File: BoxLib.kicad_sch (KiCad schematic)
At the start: 18 parts, among them J1 Generic_2Pos_terminal_block, J10 Molex_2Pos_terminal_block_1.2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, J11 Generic_2Pos_terminal_block, J2 Solder-Jumper-NO, J3 Solder-Jumper-NO, J4 Solder-Jumper-NO, J5 Solder-Jumper-NC, J6 Solder-Jumper-NC, J7 Solder-Jumper-NC, J8 Solder-Jumper-NO, J9 Solder-Jumper-NC, U1 QT_Py_RP2040, U2 QT_Py

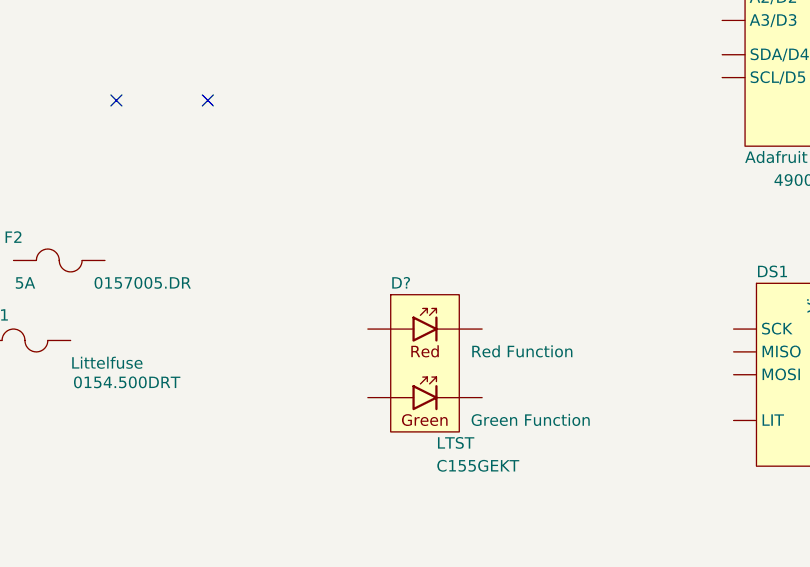
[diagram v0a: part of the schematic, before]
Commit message: Added PTH varients of devices
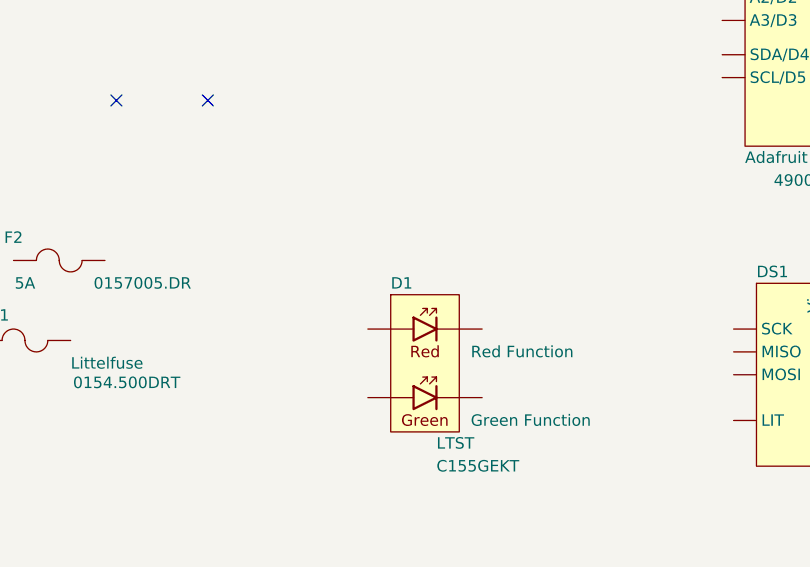
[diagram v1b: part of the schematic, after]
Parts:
- gave numbers to parts that had none: 1
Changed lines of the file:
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@@
   (symbol (lib_id "BoxLib-LEDs:LED-LTST-C155GEKT") (at 154.94 105.41 0) (unit 1)
     (in_bom yes) (on_board yes)
-    (property "Reference" "D?" (id 0) (at 151.13 96.52 0)
+    (property "Reference" "D1" (id 0) (at 151.13 96.52 0)
       (effects (font (size 1.27 1.27)) (justify left))
     )
@@
   (symbol_instances
     (path "/cfdfa8c8-35d8-45dc-a3f3-e836c8fa5543"
-      (reference "D?") (unit 1) (value "LED-LTST-C155GEKT") (footprint "BoxLib:LED-LTST-C155GEKT")
+      (reference "D1") (unit 1) (value "LED-LTST-C155GEKT") (footprint "BoxLib:LED-LTST-C155GEKT")
     )
     (path "/98ca5169-231d-4f6e-bb1a-cdb364a5a08d"
